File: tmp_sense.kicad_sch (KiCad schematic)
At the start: 0 parts

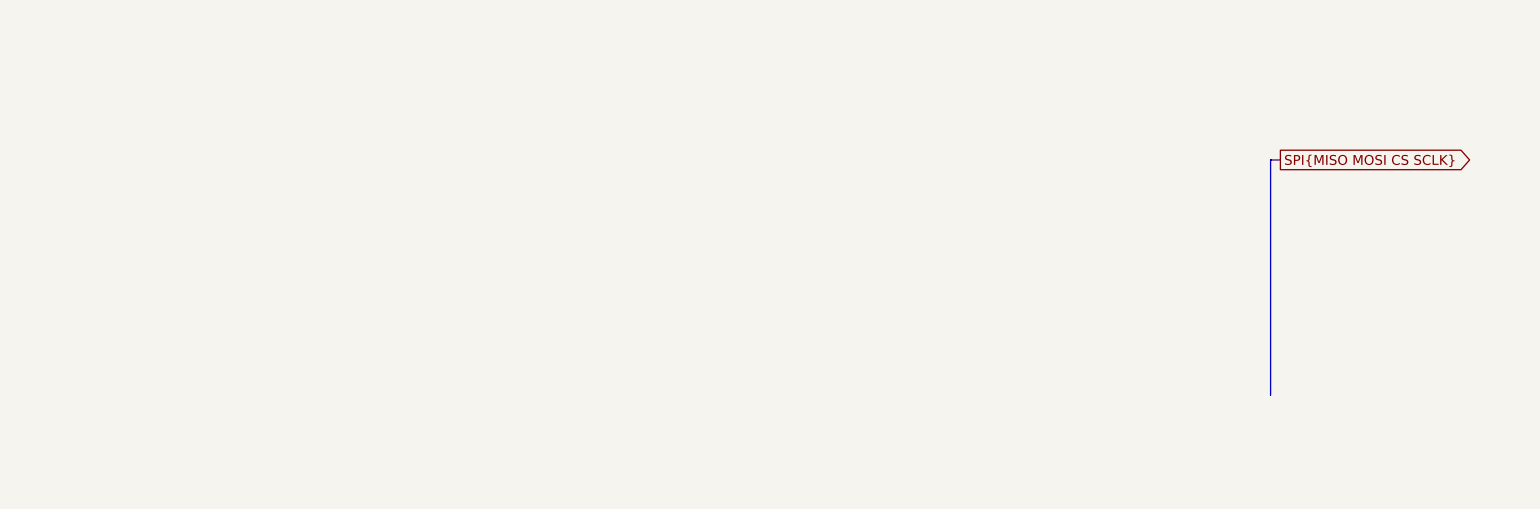
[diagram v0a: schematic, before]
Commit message: Add ADT7310 SPI temperature sensor on the temperature sheet
U7 ADT7310TRZ (SOIC-8) on the shared SPI bus: SCLK, MOSI, MISO and CS to
Teensy pins 13, 11, 12 and 10. Powered from +3V3 with C31 100n at VDD.
INT and CT are left unconnected. New ADT7310TRZ symbol in the project
library, pinout from the ADT7310 datasheet Rev. A, page 6.

Co-Authored-By: Claude Opus 5.5 (1M context) <noreply@anthropic.com>
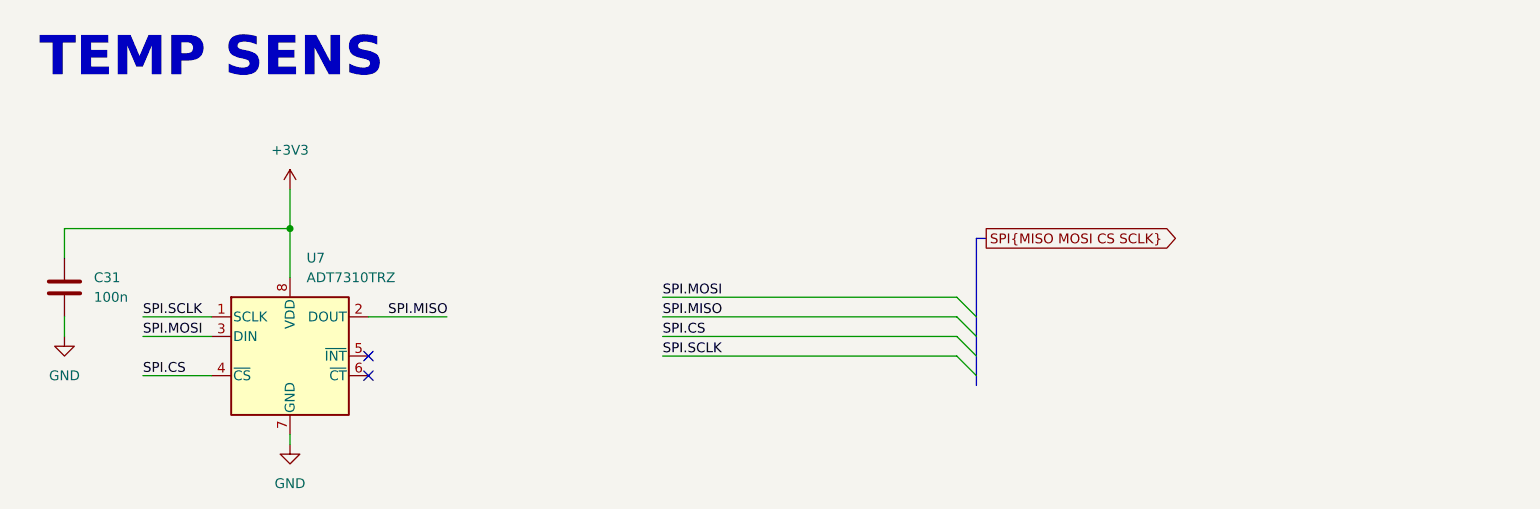
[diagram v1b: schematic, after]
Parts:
- added C31: 100n, Capacitor_SMD:C_0805_2012Metric_Pad1.18x1.45mm_HandSolder, symbol Device:C
- added U7: ADT7310TRZ, Package_SO:SOIC-8_3.9x4.9mm_P1.27mm, symbol ldo_bringup_board_ee372:ADT7310TRZ
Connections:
- new net +3V3: C31.1, U7.8 (VDD)
- new net GND: C31.2, U7.7 (GND)
- new net SPI.CS: U7.4 (~{CS})
- new net SPI.MISO: U7.2 (DOUT)
- new net SPI.MOSI: U7.3 (DIN)
- new net SPI.SCLK: U7.1 (SCLK)
- no-connect marks 0 -> 2
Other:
- note added: "TEMP SENS"
